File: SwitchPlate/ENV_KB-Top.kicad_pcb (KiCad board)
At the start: 2 copper layers, 354.6 x 156.1 mm, 8 parts

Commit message: added Gerber for optional switch plate
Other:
- board text removed: "PLEASE CHECK ALIGNMENT OF "TYPE-C-31-M-12" or "J0""
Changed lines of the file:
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@@
   (general
     (thickness 1.6)
-    (drawings 824)
+    (drawings 825)
     (tracks 0)
     (zones 0)
@@
     (pad 1 np_thru_hole circle (at 0 0) (size 3.2 3.2) (drill 3.2) (layers *.Cu *.Mask))
   )
+  (gr_arc (start 379.025 88.785) (end 379.025 91.785) (angle -90) (layer Edge.Cuts) (width 0.1))
+  (gr_line (start 382.025 62.685) (end 382.025 88.785) (layer Edge.Cuts) (width 0.1))
+  (gr_line (start 45.425 91.785) (end 379.025 91.785) (layer Edge.Cuts) (width 0.1))
+  (gr_arc (start 45.425 88.785) (end 42.425 88.785) (angle -90) (layer Edge.Cuts) (width 0.1))
+  (gr_line (start 42.425 62.685) (end 42.425 88.785) (layer Edge.Cuts) (width 0.1))
+  (gr_arc (start 39.425 62.685) (end 42.425 62.685) (angle -90) (layer Edge.Cuts) (width 0.1))
+  (gr_arc (start 385.025 62.685) (end 385.025 59.685) (angle -90) (layer Edge.Cuts) (width 0.1))
+  (dimension 339.2 (width 0.1) (layer Dwgs.User)
+    (gr_text "339.200 mm" (at 212.225 57.435) (layer Dwgs.User)
+      (effects (font (size 1 1) (thickness 0.15)))
+    )
+    (feature1 (pts (xy 381.825 59.585) (xy 381.825 58.098579)))
+    (feature2 (pts (xy 42.625 59.585) (xy 42.625 58.098579)))
+    (crossbar (pts (xy 42.625 58.685) (xy 381.825 58.685)))
+    (arrow1a (pts (xy 381.825 58.685) (xy 380.698496 59.271421)))
+    (arrow1b (pts (xy 381.825 58.685) (xy 380.698496 58.098579)))
+    (arrow2a (pts (xy 42.625 58.685) (xy 43.751504 59.271421)))
+    (arrow2b (pts (xy 42.625 58.685) (xy 43.751504 58.098579)))
+  )
+  (dimension 32.2 (width 0.1) (layer Dwgs.User)
+    (gr_text "32.200 mm" (at 41.375 75.685 90) (layer Dwgs.User)
+      (effects (font (size 1 1) (thickness 0.15)))
+    )
+    (feature1 (pts (xy 45.425 59.585) (xy 42.038579 59.585)))
+    (feature2 (pts (xy 45.425 91.785) (xy 42.038579 91.785)))
+    (crossbar (pts (xy 42.625 91.785) (xy 42.625 59.585)))
+    (arrow1a (pts (xy 42.625 59.585) (xy 43.211421 60.711504)))
+    (arrow1b (pts (xy 42.625 59.585) (xy 42.038579 60.711504)))
+    (arrow2a (pts (xy 42.625 91.785) (xy 43.211421 90.658496)))
+    (arrow2b (pts (xy 42.625 91.785) (xy 42.038579 90.658496)))
+  )
   (gr_text "https://github.com/Envious-Data/Env-KB   " (at 371.625 116.085) (layer B.Cu)
     (effects (font (size 2 2) (thickness 0.3)) (justify left mirror))
   )
-  (gr_arc (start 379.025 88.785) (end 379.025 91.785) (angle -90) (layer Edge.Cuts) (width 0.1))
-  (gr_line (start 382.025 62.685) (end 382.025 88.785) (layer Edge.Cuts) (width 0.1))
   (gr_line (start 386.525 59.685) (end 385.025 59.685) (layer Edge.Cuts) (width 0.1))
   (dimension 1.5 (width 0.1) (layer Dwgs.User)
@@
     (arrow2b (pts (xy 37.925 57.985) (xy 39.051504 57.398579)))
   )
-  (gr_arc (start 385.025 62.685) (end 385.025 59.685) (angle -90) (layer Edge.Cuts) (width 0.1))
-  (gr_line (start 45.425 91.785) (end 379.025 91.785) (layer Edge.Cuts) (width 0.1))
-  (gr_arc (start 45.425 88.785) (end 42.425 88.785) (angle -90) (layer Edge.Cuts) (width 0.1))
   (dimension 3 (width 0.1) (layer Dwgs.User)
     (gr_text "3.000 mm" (at 40.375 93.285 90) (layer Dwgs.User)
@@
     (arrow2b (pts (xy 41.625 94.785) (xy 41.038579 93.658496)))
   )
-  (gr_line (start 42.425 62.685) (end 42.425 88.785) (layer Edge.Cuts) (width 0.1))
   (gr_line (start 37.925 59.685) (end 39.425 59.685) (layer Edge.Cuts) (width 0.1))
-  (gr_arc (start 39.425 62.685) (end 42.425 62.685) (angle -90) (layer Edge.Cuts) (width 0.1))
   (gr_arc (start 292.3238 84.8494) (end 292.3238 85.3494) (angle -90) (layer Eco2.User) (width 0.1))
   (gr_line (start 292.8238 64.5094) (end 292.8238 84.8494) (layer Eco2.User) (width 0.1))
@@
     (effects (font (size 0.8 0.8) (thickness 0.155)))
   )
-  (gr_text "PLEASE CHECK ALIGNMENT OF \"TYPE-C-31-M-12\" or \"J0\"" (at 212.225 57.485) (layer F.Fab)
-    (effects (font (size 1 1) (thickness 0.15)))
-  )
   (gr_line (start 34.925 212.785) (end 34.925 62.685) (layer Edge.Cuts) (width 0.1))

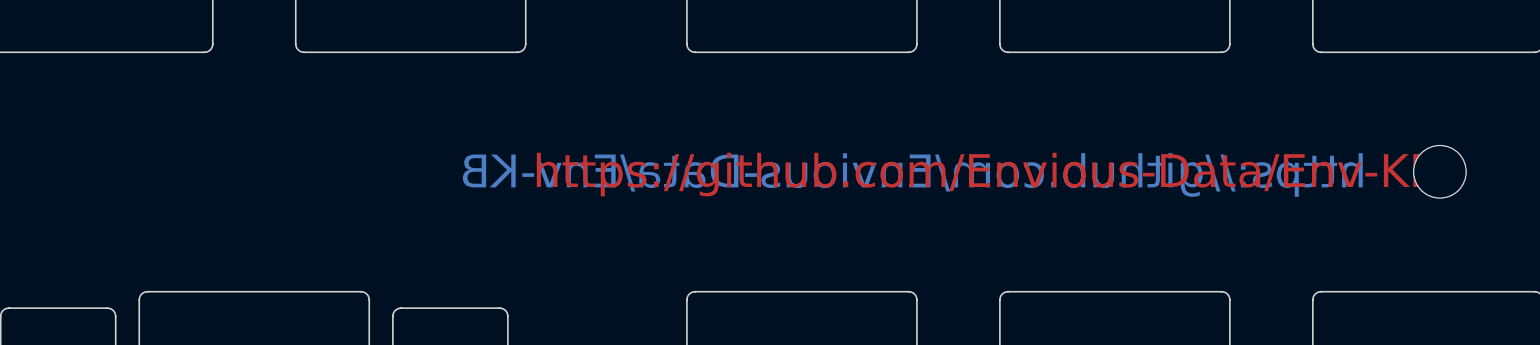
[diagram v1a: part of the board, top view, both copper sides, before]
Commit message: Corrected some netlist issues on backplate and switch plate + cleanup of stuff.
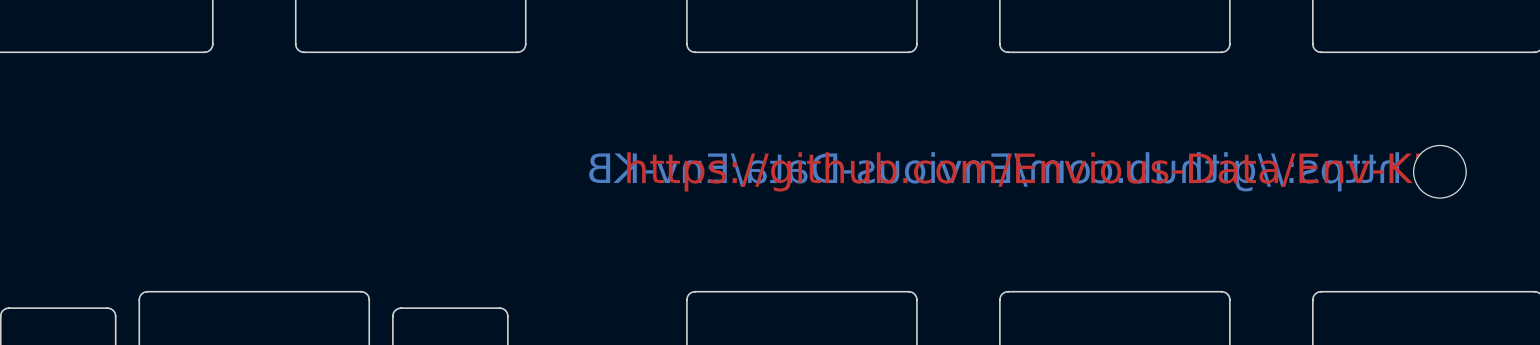
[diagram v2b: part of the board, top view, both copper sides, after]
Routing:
- added copper zone on B.Cu, net (none)
- added copper zone on F.Cu, net (none)
- removed copper zone on B.Cu, net GND
- removed copper zone on F.Cu, net GND
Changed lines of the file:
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@@
-(kicad_pcb (version 20171130) (host pcbnew "(5.1.9)-1")
+(kicad_pcb (version 20171130) (host pcbnew "(5.1.10)-1")
   (general
     (thickness 1.6)
@@
     (zones 0)
     (modules 8)
-    (nets 2)
+    (nets 1)
   )
   (page USLedger)
@@
   )
   (net 0 "")
-  (net 1 GND)
   (net_class Default "This is the default net class."
     (clearance 0.2)
@@
       (effects (font (size 1 1) (thickness 0.15)))
     )
+    (fp_circle (center 0 0) (end 3.2 0) (layer Cmts.User) (width 0.15))
     (fp_circle (center 0 0) (end 3.45 0) (layer F.CrtYd) (width 0.05))
-    (fp_circle (center 0 0) (end 3.2 0) (layer Cmts.User) (width 0.15))
     (pad 1 np_thru_hole circle (at 0 0) (size 3.2 3.2) (drill 3.2) (layers *.Cu *.Mask))
   )
@@
       (effects (font (size 1 1) (thickness 0.15)))
     )
+    (fp_circle (center 0 0) (end 3.2 0) (layer Cmts.User) (width 0.15))
     (fp_circle (center 0 0) (end 3.45 0) (layer F.CrtYd) (width 0.05))
-    (fp_circle (center 0 0) (end 3.2 0) (layer Cmts.User) (width 0.15))
     (pad 1 np_thru_hole circle (at 0 0) (size 3.2 3.2) (drill 3.2) (layers *.Cu *.Mask))
   )
@@
       (effects (font (size 1 1) (thickness 0.15)))
     )
+    (fp_circle (center 0 0) (end 3.45 0) (layer F.CrtYd) (width 0.05))
     (fp_circle (center 0 0) (end 3.2 0) (layer Cmts.User) (width 0.15))
-    (fp_circle (center 0 0) (end 3.45 0) (layer F.CrtYd) (width 0.05))
     (pad 1 np_thru_hole circle (at 0 0) (size 3.2 3.2) (drill 3.2) (layers *.Cu *.Mask))
   )
@@
       (effects (font (size 1 1) (thickness 0.15)))
     )
+    (fp_circle (center 0 0) (end 3.2 0) (layer Cmts.User) (width 0.15))
     (fp_circle (center 0 0) (end 3.45 0) (layer F.CrtYd) (width 0.05))
-    (fp_circle (center 0 0) (end 3.2 0) (layer Cmts.User) (width 0.15))
     (pad 1 np_thru_hole circle (at 0 0) (size 3.2 3.2) (drill 3.2) (layers *.Cu *.Mask))
   )
@@
       (effects (font (size 1 1) (thickness 0.15)))
     )
+    (fp_circle (center 0 0) (end 3.2 0) (layer Cmts.User) (width 0.15))
     (fp_circle (center 0 0) (end 3.45 0) (layer F.CrtYd) (width 0.05))
-    (fp_circle (center 0 0) (end 3.2 0) (layer Cmts.User) (width 0.15))
     (pad 1 np_thru_hole circle (at 0 0) (size 3.2 3.2) (drill 3.2) (layers *.Cu *.Mask))
   )
@@
       (effects (font (size 1 1) (thickness 0.15)))
     )
+    (fp_circle (center 0 0) (end 3.2 0) (layer Cmts.User) (width 0.15))
     (fp_circle (center 0 0) (end 3.45 0) (layer F.CrtYd) (width 0.05))
-    (fp_circle (center 0 0) (end 3.2 0) (layer Cmts.User) (width 0.15))
     (pad 1 np_thru_hole circle (at 0 0) (size 3.2 3.2) (drill 3.2) (layers *.Cu *.Mask))
   )
@@
       (effects (font (size 1 1) (thickness 0.15)))
     )
+    (fp_circle (center 0 0) (end 3.45 0) (layer F.CrtYd) (width 0.05))
     (fp_circle (center 0 0) (end 3.2 0) (layer Cmts.User) (width 0.15))
-    (fp_circle (center 0 0) (end 3.45 0) (layer F.CrtYd) (width 0.05))
     (pad 1 np_thru_hole circle (at 0 0) (size 3.2 3.2) (drill 3.2) (layers *.Cu *.Mask))
   )
@@
       (effects (font (size 1 1) (thickness 0.15)))
     )
+    (fp_circle (center 0 0) (end 3.2 0) (layer Cmts.User) (width 0.15))
     (fp_circle (center 0 0) (end 3.45 0) (layer F.CrtYd) (width 0.05))
-    (fp_circle (center 0 0) (end 3.2 0) (layer Cmts.User) (width 0.15))
     (pad 1 np_thru_hole circle (at 0 0) (size 3.2 3.2) (drill 3.2) (layers *.Cu *.Mask))
+  )
+  (gr_text "   https://github.com/Envious-Data/Env-KB" (at 376.168 115.909) (layer B.Cu)
+    (effects (font (size 1.8 1.8) (thickness 0.3)) (justify left mirror))
   )
   (gr_arc (start 379.025 88.785) (end 379.025 91.785) (angle -90) (layer Edge.Cuts) (width 0.1))
@@
     (arrow2a (pts (xy 42.625 91.785) (xy 43.211421 90.658496)))
     (arrow2b (pts (xy 42.625 91.785) (xy 42.038579 90.658496)))
-  )
-  (gr_text "https://github.com/Envious-Data/Env-KB   " (at 371.625 116.085) (layer B.Cu)
-    (effects (font (size 2 2) (thickness 0.3)) (justify left mirror))
   )
   (gr_line (start 386.525 59.685) (end 385.025 59.685) (layer Edge.Cuts) (width 0.1))
@@
   (gr_line (start 34.925 212.785) (end 34.925 62.685) (layer Edge.Cuts) (width 0.1))
   (gr_line (start 386.525 215.785) (end 37.925 215.785) (layer Edge.Cuts) (width 0.1))
-  (gr_text "https://github.com/Envious-Data/Env-KB   " (at 376.075 116.06) (layer F.Cu)
-    (effects (font (size 2 2) (thickness 0.3)) (justify right))
-  )
-  (zone (net 1) (net_name GND) (layer F.Cu) (hatch edge 0.508)
+  (gr_text "https://github.com/Envious-Data/Env-KB   " (at 376.075 115.915) (layer F.Cu)
+    (effects (font (size 1.8 1.8) (thickness 0.3)) (justify right))
+  )
+  (zone (net 0) (net_name "") (layer F.Cu) (hatch edge 0.508)
     (connect_pads yes (clearance 0.508))
     (min_thickness 0.254)
@@
     )
   )
-  (zone (net 1) (net_name GND) (layer B.Cu) (hatch edge 0.508)
+  (zone (net 0) (net_name "") (layer B.Cu) (hatch edge 0.508)
     (connect_pads yes (clearance 0.508))
     (min_thickness 0.254)

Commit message: updated some bits namely R1 keymap
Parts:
- H0, H1, H10, H3, H4, H6, H7, H9: footprint MountingHole:MountingHole_3.2mm_M3 -> mounthole:MountingHole_3.2mm_M3_modified
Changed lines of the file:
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@@
     (visible_elements 7FFFFFFF)
     (pcbplotparams
-      (layerselection 0x010fc_ffffffff)
+      (layerselection 0x00400_7ffffffe)
       (usegerberextensions true)
       (usegerberattributes false)
       (usegerberadvancedattributes false)
       (creategerberjobfile false)
-      (excludeedgelayer true)
+      (excludeedgelayer false)
       (linewidth 0.150000)
       (plotframeref false)
@@
       (psnegative false)
       (psa4output false)
-      (plotreference true)
+      (plotreference false)
       (plotvalue false)
       (plotinvisibletext false)
       (padsonsilk false)
       (subtractmaskfromsilk true)
-      (outputformat 1)
+      (outputformat 3)
       (mirror false)
       (drillshape 0)
@@
     (diff_pair_gap 0.1778)
   )
-  (module MountingHole:MountingHole_3.2mm_M3 (layer F.Cu)
+  (module mounthole:MountingHole_3.2mm_M3_modified (layer F.Cu)
     (at 376.075 116.06)
     (descr "Mounting Hole 3.2mm, no annular, M3")
     (tags "mounting hole 3.2mm no annular m3")
     (attr virtual)
-    (fp_text reference H10 (at 0 -4.2) (layer Dwgs.User) hide
+    (fp_text reference H10 (at 0 -4.2) (layer Dwgs.User)
       (effects (font (size 1 1) (thickness 0.15)))
     )
@@
       (effects (font (size 1 1) (thickness 0.15)))
     )
+    (fp_circle (center 0 0) (end 1.504605 0.34) (layer Eco1.User) (width 0.12))
     (fp_circle (center 0 0) (end 3.2 0) (layer Cmts.User) (width 0.15))
     (fp_circle (center 0 0) (end 3.45 0) (layer F.CrtYd) (width 0.05))
     (pad 1 np_thru_hole circle (at 0 0) (size 3.2 3.2) (drill 3.2) (layers *.Cu *.Mask))
   )
-  (module MountingHole:MountingHole_3.2mm_M3 (layer F.Cu)
+  (module mounthole:MountingHole_3.2mm_M3_modified (layer F.Cu)
     (at 48.375 116.06)
     (descr "Mounting Hole 3.2mm, no annular, M3")
     (tags "mounting hole 3.2mm no annular m3")
     (attr virtual)
-    (fp_text reference H9 (at 0 -4.2) (layer Dwgs.User) hide
+    (fp_text reference H9 (at 0 -4.2) (layer Dwgs.User)
       (effects (font (size 1 1) (thickness 0.15)))
     )
@@
       (effects (font (size 1 1) (thickness 0.15)))
     )
+    (fp_circle (center 0 0) (end 1.504605 0.34) (layer Eco1.User) (width 0.12))
     (fp_circle (center 0 0) (end 3.2 0) (layer Cmts.User) (width 0.15))
     (fp_circle (center 0 0) (end 3.45 0) (layer F.CrtYd) (width 0.05))
     (pad 1 np_thru_hole circle (at 0 0) (size 3.2 3.2) (drill 3.2) (layers *.Cu *.Mask))
   )
-  (module MountingHole:MountingHole_3.2mm_M3 (layer F.Cu)
+  (module mounthole:MountingHole_3.2mm_M3_modified (layer F.Cu)
     (at 209.225 210.185)
     (descr "Mounting Hole 3.2mm, no annular, M3")
@@
       (effects (font (size 1 1) (thickness 0.15)))
     )
+    (fp_circle (center 0 0) (end 1.504605 0.34) (layer Eco1.User) (width 0.12))
+    (fp_circle (center 0 0) (end 3.2 0) (layer Cmts.User) (width 0.15))
     (fp_circle (center 0 0) (end 3.45 0) (layer F.CrtYd) (width 0.05))
-    (fp_circle (center 0 0) (end 3.2 0) (layer Cmts.User) (width 0.15))
     (pad 1 np_thru_hole circle (at 0 0) (size 3.2 3.2) (drill 3.2) (layers *.Cu *.Mask))
   )
-  (module MountingHole:MountingHole_3.2mm_M3 (layer F.Cu)
+  (module mounthole:MountingHole_3.2mm_M3_modified (layer F.Cu)
+    (at 385.925 212.085)
+    (descr "Mounting Hole 3.2mm, no annular, M3")
+    (tags "mounting hole 3.2mm no annular m3")
+    (attr virtual)
+    (fp_text reference H4 (at 0 -4.2) (layer Dwgs.User)
+      (effects (font (size 1 1) (thickness 0.15)))
+    )
+    (fp_text value MountingHole (at 0 4.2) (layer F.Fab)
+      (effects (font (size 1 1) (thickness 0.15)))
+    )
+    (fp_circle (center 0 0) (end 1.504605 0.34) (layer Eco1.User) (width 0.12))
+    (fp_circle (center 0 0) (end 3.2 0) (layer Cmts.User) (width 0.15))
+    (fp_circle (center 0 0) (end 3.45 0) (layer F.CrtYd) (width 0.05))
+    (pad 1 np_thru_hole circle (at 0 0) (size 3.2 3.2) (drill 3.2) (layers *.Cu *.Mask))
+  )
+  (module mounthole:MountingHole_3.2mm_M3_modified (layer F.Cu)
+    (at 38.525 212.185)
+    (descr "Mounting Hole 3.2mm, no annular, M3")
+    (tags "mounting hole 3.2mm no annular m3")
+    (attr virtual)
+    (fp_text reference H3 (at 0 -4.2) (layer Dwgs.User)
+      (effects (font (size 1 1) (thickness 0.15)))
+    )
+    (fp_text value MountingHole (at 0 4.2) (layer F.Fab)
+      (effects (font (size 1 1) (thickness 0.15)))
+    )
+    (fp_circle (center 0 0) (end 1.504605 0.34) (layer Eco1.User) (width 0.12))
+    (fp_circle (center 0 0) (end 3.2 0) (layer Cmts.User) (width 0.15))
+    (fp_circle (center 0 0) (end 3.45 0) (layer F.CrtYd) (width 0.05))
+    (pad 1 np_thru_hole circle (at 0 0) (size 3.2 3.2) (drill 3.2) (layers *.Cu *.Mask))
+  )
+  (module mounthole:MountingHole_3.2mm_M3_modified (layer F.Cu)
+    (at 385.825 63.385)
+    (descr "Mounting Hole 3.2mm, no annular, M3")
+    (tags "mounting hole 3.2mm no annular m3")
+    (attr virtual)
+    (fp_text reference H1 (at 0 -4.2) (layer Dwgs.User)
+      (effects (font (size 1 1) (thickness 0.15)))
+    )
+    (fp_text value MountingHole (at 0 4.2) (layer F.Fab)
+      (effects (font (size 1 1) (thickness 0.15)))
+    )
+    (fp_circle (center 0 0) (end 1.504605 0.34) (layer Eco1.User) (width 0.12))
+    (fp_circle (center 0 0) (end 3.2 0) (layer Cmts.User) (width 0.15))
+    (fp_circle (center 0 0) (end 3.45 0) (layer F.CrtYd) (width 0.05))
+    (pad 1 np_thru_hole circle (at 0 0) (size 3.2 3.2) (drill 3.2) (layers *.Cu *.Mask))
+  )
+  (module mounthole:MountingHole_3.2mm_M3_modified (layer F.Cu)
+    (at 38.625 63.385)
+    (descr "Mounting Hole 3.2mm, no annular, M3")
+    (tags "mounting hole 3.2mm no annular m3")
+    (attr virtual)
+    (fp_text reference H0 (at 0 -4.2) (layer Dwgs.User)
+      (effects (font (size 1 1) (thickness 0.15)))
+    )
+    (fp_text value MountingHole (at 0 4.2) (layer F.Fab)
+      (effects (font (size 1 1) (thickness 0.15)))
+    )
+    (fp_circle (center 0 0) (end 1.504605 0.34) (layer Eco1.User) (width 0.12))
+    (fp_circle (center 0 0) (end 3.2 0) (layer Cmts.User) (width 0.15))
+    (fp_circle (center 0 0) (end 3.45 0) (layer F.CrtYd) (width 0.05))
+    (pad 1 np_thru_hole circle (at 0 0) (size 3.2 3.2) (drill 3.2) (layers *.Cu *.Mask))
+  )
+  (module mounthole:MountingHole_3.2mm_M3_modified (layer F.Cu)
     (at 212.225 116.235)
     (descr "Mounting Hole 3.2mm, no annular, M3")
@@
       (effects (font (size 1 1) (thickness 0.15)))
     )
+    (fp_circle (center 0 0) (end 3.45 0) (layer F.CrtYd) (width 0.05))
     (fp_circle (center 0 0) (end 3.2 0) (layer Cmts.User) (width 0.15))
-    (fp_circle (center 0 0) (end 3.45 0) (layer F.CrtYd) (width 0.05))
+    (fp_circle (center 0 0) (end 1.504605 0.34) (layer Eco1.User) (width 0.12))
     (pad 1 np_thru_hole circle (at 0 0) (size 3.2 3.2) (drill 3.2) (layers *.Cu *.Mask))
   )
-  (module MountingHole:MountingHole_3.2mm_M3 (layer F.Cu)
-    (at 385.925 212.085)
-    (descr "Mounting Hole 3.2mm, no annular, M3")
-    (tags "mounting hole 3.2mm no annular m3")
-    (attr virtual)
-    (fp_text reference H4 (at 0 -4.2) (layer Dwgs.User) hide
-      (effects (font (size 1 1) (thickness 0.15)))
-    )
-    (fp_text value MountingHole (at 0 4.2) (layer F.Fab)
-      (effects (font (size 1 1) (thickness 0.15)))
-    )
-    (fp_circle (center 0 0) (end 3.2 0) (layer Cmts.User) (width 0.15))
-    (fp_circle (center 0 0) (end 3.45 0) (layer F.CrtYd) (width 0.05))
-    (pad 1 np_thru_hole circle (at 0 0) (size 3.2 3.2) (drill 3.2) (layers *.Cu *.Mask))
-  )
-  (module MountingHole:MountingHole_3.2mm_M3 (layer F.Cu)
-    (at 38.525 212.185)
-    (descr "Mounting Hole 3.2mm, no annular, M3")
-    (tags "mounting hole 3.2mm no annular m3")
-    (attr virtual)
-    (fp_text reference H3 (at 0 -4.2) (layer Dwgs.User) hide
-      (effects (font (size 1 1) (thickness 0.15)))
-    )
-    (fp_text value MountingHole (at 0 4.2) (layer F.Fab)
-      (effects (font (size 1 1) (thickness 0.15)))
-    )
-    (fp_circle (center 0 0) (end 3.2 0) (layer Cmts.User) (width 0.15))
-    (fp_circle (center 0 0) (end 3.45 0) (layer F.CrtYd) (width 0.05))
-    (pad 1 np_thru_hole circle (at 0 0) (size 3.2 3.2) (drill 3.2) (layers *.Cu *.Mask))
-  )
-  (module MountingHole:MountingHole_3.2mm_M3 (layer F.Cu)
-    (at 385.825 63.385)
-    (descr "Mounting Hole 3.2mm, no annular, M3")
-    (tags "mounting hole 3.2mm no annular m3")
-    (attr virtual)
-    (fp_text reference H1 (at 0 -4.2) (layer Dwgs.User) hide
-      (effects (font (size 1 1) (thickness 0.15)))
-    )
-    (fp_text value MountingHole (at 0 4.2) (layer F.Fab)
-      (effects (font (size 1 1) (thickness 0.15)))
-    )
-    (fp_circle (center 0 0) (end 3.45 0) (layer F.CrtYd) (width 0.05))
-    (fp_circle (center 0 0) (end 3.2 0) (layer Cmts.User) (width 0.15))
-    (pad 1 np_thru_hole circle (at 0 0) (size 3.2 3.2) (drill 3.2) (layers *.Cu *.Mask))
-  )
-  (module MountingHole:MountingHole_3.2mm_M3 (layer F.Cu)
-    (at 38.625 63.385)
-    (descr "Mounting Hole 3.2mm, no annular, M3")
-    (tags "mounting hole 3.2mm no annular m3")
-    (attr virtual)
-    (fp_text reference H0 (at 0 -4.2) (layer Dwgs.User) hide
-      (effects (font (size 1 1) (thickness 0.15)))
-    )
-    (fp_text value MountingHole (at 0 4.2) (layer F.Fab)
-      (effects (font (size 1 1) (thickness 0.15)))
-    )
-    (fp_circle (center 0 0) (end 3.2 0) (layer Cmts.User) (width 0.15))
-    (fp_circle (center 0 0) (end 3.45 0) (layer F.CrtYd) (width 0.05))
-    (pad 1 np_thru_hole circle (at 0 0) (size 3.2 3.2) (drill 3.2) (layers *.Cu *.Mask))
-  )

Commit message: Changed all mount holes to M2 and added some pads around the holes to avoid scratches being visible on pcbs
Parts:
- H0, H1, H10, H3, H4, H6, H7, H9: footprint mounthole:MountingHole_3.2mm_M3_modified -> MountingHole:MountingHole_2.2mm_M2_Pad
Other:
- board text removed: "Envious.Media"

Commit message: updated switch plate(s) to include a slot for installing pcb mount stabs
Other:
- outline, holes or cut-outs redrawn
